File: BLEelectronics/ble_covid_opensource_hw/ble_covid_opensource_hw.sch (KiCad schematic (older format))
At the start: 36 parts, among them IC1 LTC4412xS6, IC2 PCF8523T, IC3 MX25R6435FM2IL0, IC4 LTC4054LES5-4.2#TRPBF, J1 USB_A_PLUG, J4 Conn_01x01_Female, Q1 Si2307CDS, Q2 Si7463DP, U1 LP5907MFX-3.3, U2 BAT-HLD-001, U3 ESD401, U4 ESD401, U5 TPD2E2U06

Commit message: Schematic draft, working on Antenna layout.
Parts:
- added J2: USB_B_Micro, Connector_USB:USB_Micro-B_Molex-105017-0001, symbol Connector:USB_B_Micro
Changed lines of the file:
@@
 	0    -1   1    0
 $EndComp
+$Comp
+L Connector:USB_B_Micro J2
+U 1 1 5EC90B66
+P 2850 7100
+F 0 "J2" H 2907 7567 50  0000 C CNN
+F 1 "USB_B_Micro" H 2907 7476 50  0000 C CNN
+F 2 "Connector_USB:USB_Micro-B_Molex-105017-0001" H 3000 7050 50  0001 C CNN
+F 3 "https://www.molex.com/pdm_docs/sd/1050170001_sd.pdf" H 3000 7050 50  0001 C CNN
+F 4 "Molex" H 2850 7100 50  0001 C CNN "MFR"
+F 5 "1050170001" H 2850 7100 50  0001 C CNN "MPN"
+F 6 "WM1399CT-ND" H 2850 7100 50  0001 C CNN "DPN"
+	1    2850 7100
+	1    0    0    -1
+$EndComp
 $EndSCHEMATC

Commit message: Partial progress on hw mvp 1b.
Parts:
- removed J1: USB_A_PLUG, 0my_footprints:usbA-PCB, symbol usb_a_plug:USB_A_PLUG
- removed JP1, JP2, JP4: Jumper_2_Open, Jumper:SolderJumper-2_P1.3mm_Open_RoundedPad1.0x1.5mm, symbol Jumper:Jumper_2_Open
- removed Q2: Si7463DP, Package_SO:PowerPAK_SO-8_Single, symbol Si7463DP:Si7463DP
- removed R2, R3: 0, Resistor_SMD:R_0603_1608Metric_Pad1.05x0.95mm_HandSolder, symbol Device:R
- added C23: 4.7uF, Capacitor_SMD:C_0603_1608Metric_Pad1.05x0.95mm_HandSolder, symbol Device:C
- R8, R9: value 4.7K -> 10K
- U5: footprint Package_TO_SOT_SMD:SOT-543 -> Package_TO_SOT_SMD:SOT-553
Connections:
- no-connect marks 6 -> 7
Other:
- note added: "ESD protection on USB data"
- moved on the sheet: C1, C2, C4, C5, D3, IC2, J2, J4, JP3, Q1, R1, R4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

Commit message: Remove rescue cache references.
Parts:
- IC1: symbol CR2025_Nordic-rescue:LTC4412xS6-ltc4412xs6 -> ltc4412xs6:LTC4412xS6
- IC3: symbol CR2025_Nordic-rescue:MX25R6435FM2IL0-mx25R6435FM2IL -> mx25R6435FM2IL:MX25R6435FM2IL0
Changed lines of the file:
@@
 $EndComp
 $Comp
-L CR2025_Nordic-rescue:MX25R6435FM2IL0-mx25R6435FM2IL IC3
+L mx25R6435FM2IL:MX25R6435FM2IL0 IC3
 U 1 1 5E9F9A1A
 P 8750 5400
@@
 	4400 4350 4600 4350
 $Comp
-L CR2025_Nordic-rescue:LTC4412xS6-ltc4412xs6 IC1
+L ltc4412xs6:LTC4412xS6 IC1
 U 1 1 5E9DE63A
 P 2550 5650

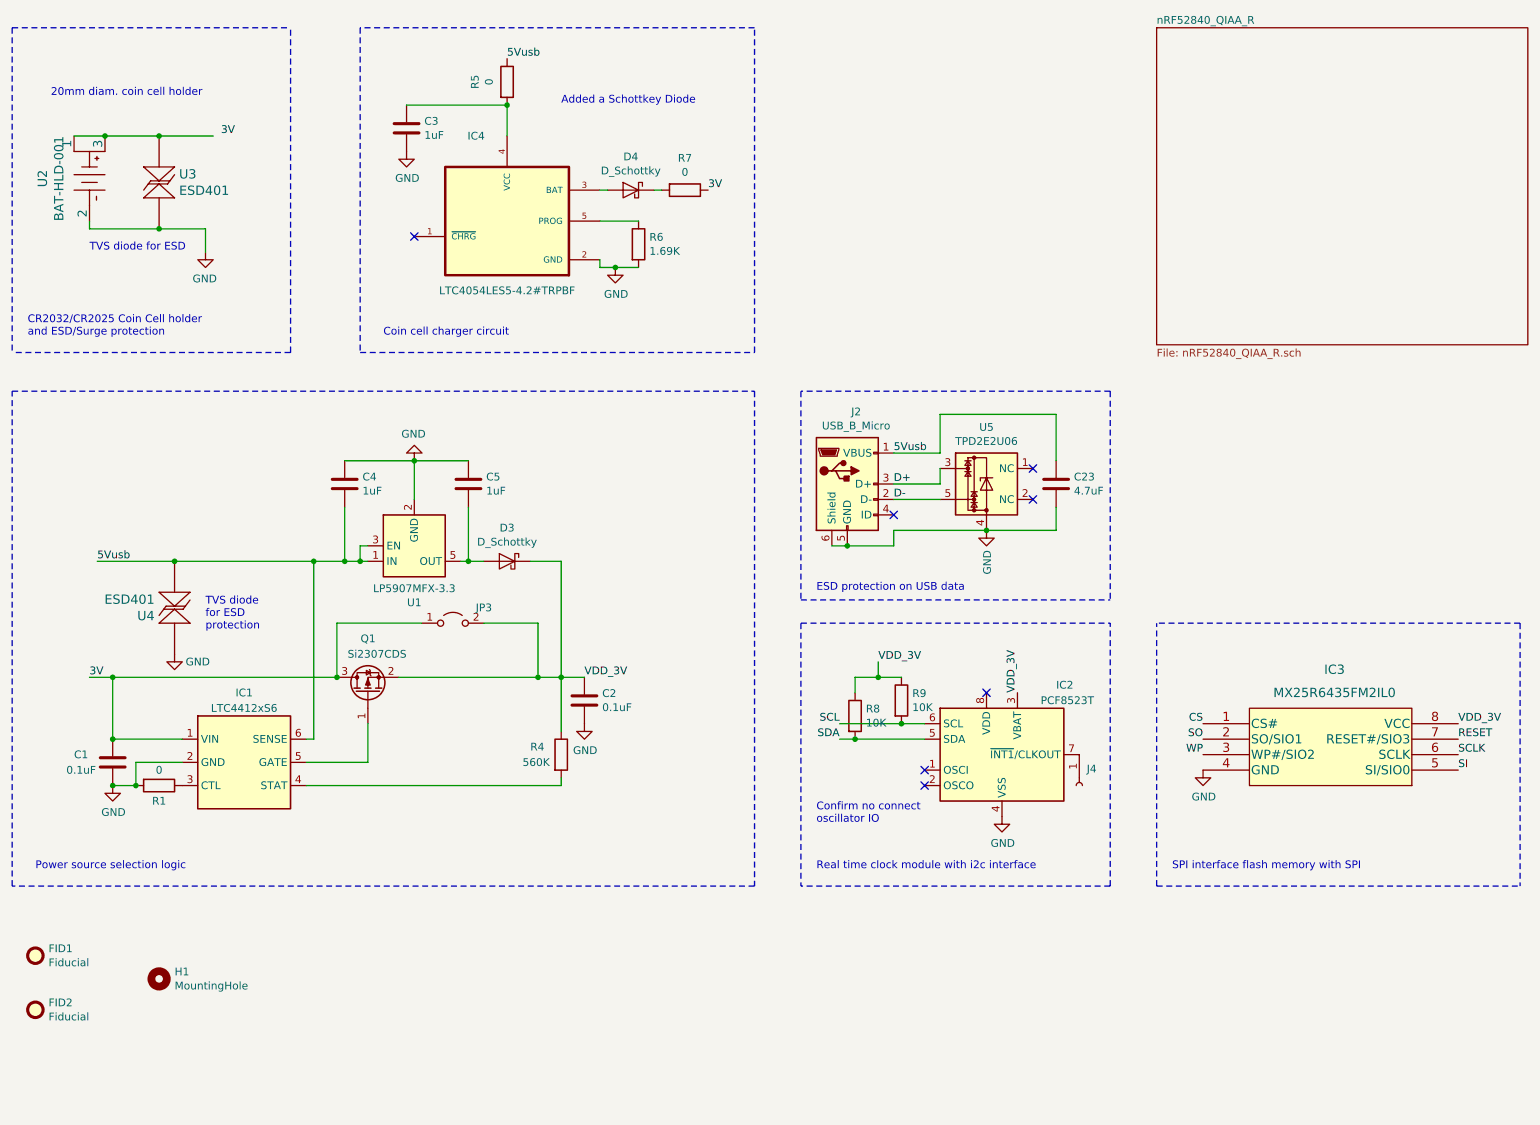
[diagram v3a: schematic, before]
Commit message: MVP 1b schematic almost ready for review.
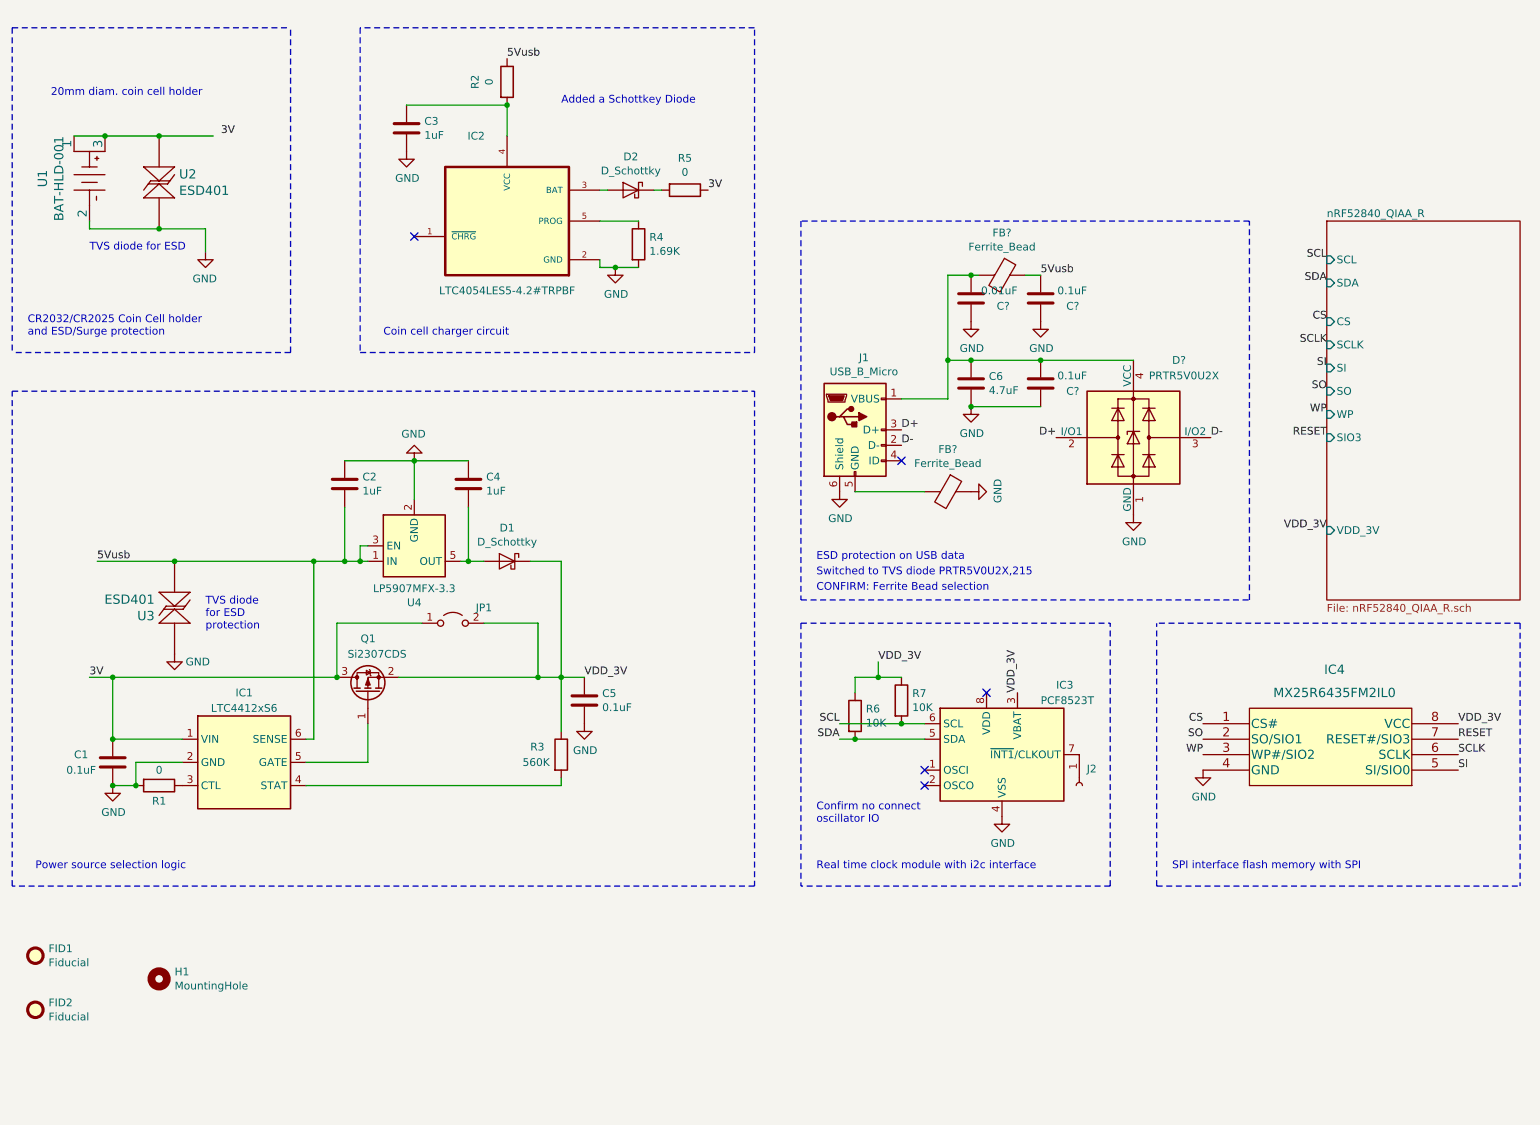
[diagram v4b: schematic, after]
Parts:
- removed U5: TPD2E2U06, Package_TO_SOT_SMD:SOT-553, symbol Power_Protection:TPD2E2U06
- added C? (x2): 0.1uF, Capacitor_SMD:C_0603_1608Metric_Pad1.05x0.95mm_HandSolder, symbol Device:C
- added C?: 0.01uF, Capacitor_SMD:C_0603_1608Metric_Pad1.05x0.95mm_HandSolder, symbol Device:C
- added D?: PRTR5V0U2X, Package_TO_SOT_SMD:SOT-143, symbol Power_Protection:PRTR5V0U2X
- added FB? (x2): Ferrite_Bead, Inductor_SMD:L_0402_1005Metric, symbol Device:Ferrite_Bead
- renumbered C4 to C2, C5 to C4, C2 to C5, C23 to C6, D3 to D1, D4 to D2, IC4 to IC2, IC2 to IC3, IC3 to IC4, J2 to J1, J4 to J2, JP3 to JP1, R5 to R2, R4 to R3, R6 to R4, R7 to R5, R8 to R6, R9 to R7, U2 to U1, U3 to U2, U4 to U3, U1 to U4
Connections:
- net 5Vusb: now also C?.2, FB?.1; no longer C6.1, J1.1 (VBUS)
- net D+: now also D?.2 (I/O1)
- net D-: now also D?.3 (I/O2)
- net GND: now also C?.1, C?.1, C?.1, D?.1 (GND), FB?.1; no longer J1.5 (GND)
- new net: C6.1, C?.2, C?.2, D?.4 (VCC), FB?.2, J1.1 (VBUS)
- new net: FB?.2, J1.5 (GND)
- no-connect marks 7 -> 5
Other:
- note added: "CONFIRM: Ferrite Bead selection"
- note added: "Switched to TVS diode PRTR5V0U2X,215"
- moved on the sheet: C6, J1

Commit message: hw mvp 1b schematic full draft ready for review
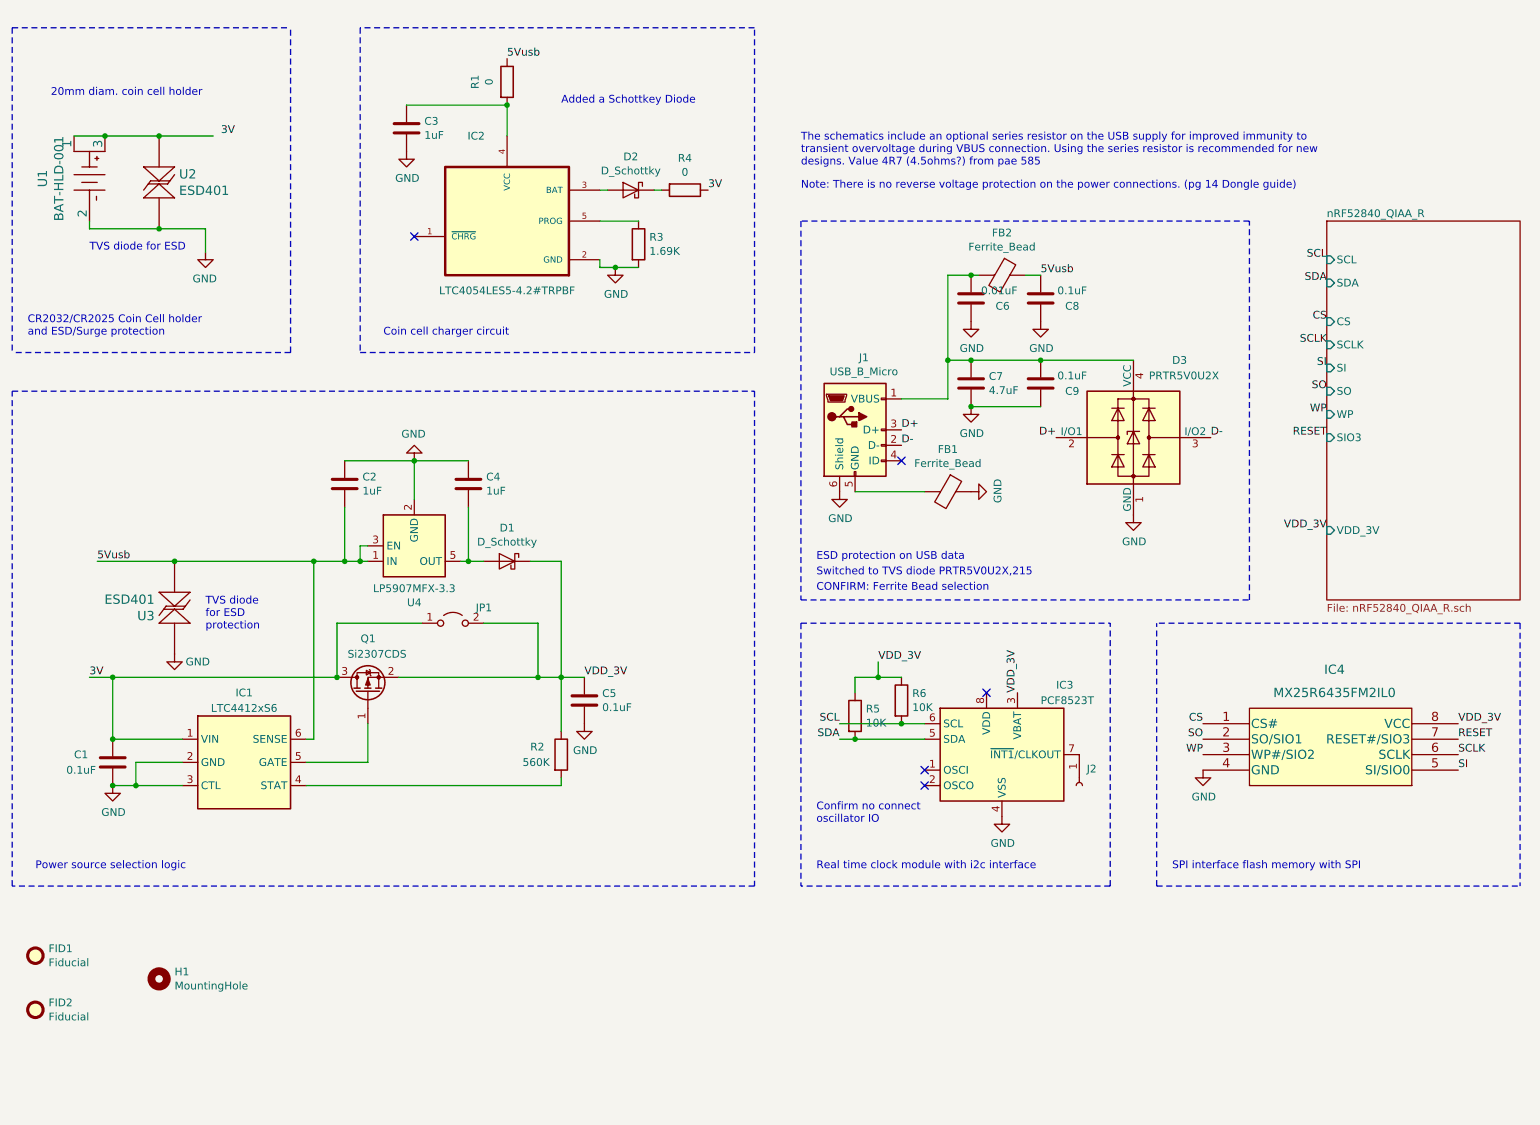
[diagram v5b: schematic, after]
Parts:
- removed R1: 0, Resistor_SMD:R_0603_1608Metric_Pad1.05x0.95mm_HandSolder, symbol Device:R
- C1: footprint Capacitor_SMD:C_0603_1608Metric_Pad1.05x0.95mm_HandSolder -> Capacitor_SMD:C_0402_1005Metric
- C2: footprint Capacitor_SMD:C_0603_1608Metric_Pad1.05x0.95mm_HandSolder -> Capacitor_SMD:C_0402_1005Metric; DPN 1276-1862-1-ND -> (none); MFR Samsung -> (none); MPN CL10A105KO5LNNC -> (none)
- C4: footprint Capacitor_SMD:C_0603_1608Metric_Pad1.05x0.95mm_HandSolder -> Capacitor_SMD:C_0402_1005Metric; MFR Samsung -> (none); MPN CL10A105KO5LNNC -> (none)
- C6, C8, C9: renamed from C?; footprint Capacitor_SMD:C_0603_1608Metric_Pad1.05x0.95mm_HandSolder -> Capacitor_SMD:C_0201_0603Metric
- C7: renamed from C6; footprint Capacitor_SMD:C_0603_1608Metric_Pad1.05x0.95mm_HandSolder -> Capacitor_SMD:C_0402_1005Metric
- R3: renamed from R4; footprint Resistor_SMD:R_0603_1608Metric_Pad1.05x0.95mm_HandSolder -> Resistor_SMD:R_0402_1005Metric; DPN YAG2487CT-ND -> (none); MFR Yageo -> (none); MPN RC0201FR-071K69L -> (none)
- R5: renamed from R6; footprint Resistor_SMD:R_0603_1608Metric_Pad1.05x0.95mm_HandSolder -> Resistor_SMD:R_0402_1005Metric
- R6: renamed from R7; footprint Resistor_SMD:R_0603_1608Metric_Pad1.05x0.95mm_HandSolder -> Resistor_SMD:R_0402_1005Metric
- gave numbers to parts that had none: 3
- renumbered R2 to R1, R3 to R2, R5 to R4
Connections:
- net GND: now also IC1.3 (CTL)
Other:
- note added: "Note: There is no reverse voltage protection on the power connections. (pg 14 Dongle guide)"
- note added: "The schematics include an optional series resistor on the USB supply for improved immunity to\ntransient overvoltage during VBUS connection. Using the series resistor is recommended for new\ndesigns. Value 4R7 (4.5ohms?) from pae 585"
